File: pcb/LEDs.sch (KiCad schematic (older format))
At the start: 15 parts

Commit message: almost finished with pcb design
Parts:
- removed MATRIX? (x2): LED_8X8, symbol LED_8X8
- removed U? (x3): ULN2804A, symbol ULN2804A
- added MATRIX2, MATRIX3, MATRIX4: LED_8X8, symbol LED_8X8
- added RR17, RR18, RR19, RR20, RR21, RR22, RR23, RR24: 15, symbol R
- added U2: ULN2804A, symbol ULN2804A
- RR10, RR11, RR12, RR13, RR14, RR15, RR16, RR9: renamed from R?; value 82 -> 15
- gave numbers to parts that had none: 2
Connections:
- net labels added: C0, C1, C10, C11, C12, C13, C14, C2, C3, C4, C5, C6, C7, C8, C9, R0, R1, R2, R3, R4, R5, R6, R7
- wire segments 37 -> 118
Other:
- moved on the sheet: RR10, RR11, RR12, RR13, RR14, RR15, RR16, RR9, U1

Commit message: working on power circuitry
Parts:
- removed MATRIX1, MATRIX2, MATRIX3, MATRIX4: LED_8X8, symbol LED_8X8
- added MATRIX1: LED_16X16, symbol LED_16X16
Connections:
- wire segments 118 -> 86
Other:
- moved on the sheet: RR10, RR11, RR12, RR13, RR14, RR15, RR16, RR17, RR18, RR19, RR20, RR21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

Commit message: Work on single PCB version.
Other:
- moved on the sheet: U2
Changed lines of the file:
@@
-EESchema Schematic File Version 2  date Tue 12 Mar 2013 12:56:47 AM PDT
+EESchema Schematic File Version 2  date Tue 12 Mar 2013 12:36:21 PM PDT
 LIBS:power
 LIBS:device
@@
 LIBS:leaf
 LIBS:led_16x16
+LIBS:uA7800
 LIBS:panels_g4-cache
 EELAYER 25  0
@@
 Comment4 ""
 $EndDescr
+Wire Wire Line
+	3360 5480 3710 5480
+Wire Wire Line
+	7510 3185 7255 3185
+Wire Wire Line
+	7510 2985 7255 2985
+Wire Wire Line
+	7255 2785 7510 2785
+Wire Wire Line
+	7255 2585 7510 2585
+Wire Wire Line
+	7510 2685 7255 2685
+Wire Wire Line
+	7510 2885 7255 2885
+Wire Wire Line
+	7510 3085 7255 3085
+Wire Wire Line
+	7510 3285 7255 3285
+Wire Wire Line
+	7510 4085 7255 4085
+Wire Wire Line
+	7510 3885 7255 3885
+Wire Wire Line
+	7510 3685 7255 3685
+Wire Wire Line
+	7510 3485 7255 3485
+Wire Wire Line
+	7255 3385 7510 3385
+Wire Wire Line
+	7255 3585 7510 3585
+Wire Wire Line
+	7510 3785 7255 3785
+Wire Wire Line
+	7510 3985 7255 3985
+Wire Wire Line
+	3255 3385 3695 3385
+Wire Wire Line
+	5415 6150 5415 5980
+Wire Wire Line
+	5415 5980 5310 5980
+Wire Wire Line
+	4195 2685 4755 2685
+Wire Wire Line
+	4195 2785 4755 2785
+Wire Wire Line
+	4195 2985 4755 2985
+Wire Wire Line
+	4195 3085 4755 3085
+Wire Wire Line
+	4755 3185 4195 3185
+Wire Wire Line
+	4195 3285 4755 3285
+Wire Wire Line
+	4195 2885 4755 2885
+Wire Wire Line
+	4195 2585 4755 2585
+Wire Wire Line
+	3270 2585 3695 2585
+Wire Wire Line
+	3270 2685 3695 2685
+Wire Wire Line
+	3270 2785 3695 2785
+Wire Wire Line
+	3270 3085 3695 3085
+Wire Wire Line
+	3270 2985 3695 2985
+Wire Wire Line
+	3270 2885 3695 2885
+Wire Wire Line
+	3270 3185 3695 3185
+Wire Wire Line
+	3270 3285 3695 3285
+Wire Wire Line
+	3360 5880 3710 5880
+Wire Wire Line
+	3360 5780 3710 5780
+Wire Wire Line
+	3710 5580 3360 5580
+Wire Wire Line
+	3360 5680 3710 5680
+Wire Wire Line
+	3710 5380 3360 5380
+Wire Wire Line
+	3710 5280 3360 5280
+Wire Wire Line
+	3710 5180 3360 5180
+Wire Wire Line
+	5565 5880 5310 5880
+Wire Wire Line
+	5565 5680 5310 5680
+Wire Wire Line
+	5565 5480 5310 5480
+Wire Wire Line
+	5565 5280 5310 5280
+Wire Wire Line
+	5310 5180 5565 5180
+Wire Wire Line
+	5310 5380 5565 5380
+Wire Wire Line
+	5565 5580 5310 5580
+Wire Wire Line
+	5565 5780 5310 5780
+Wire Wire Line
+	4510 6580 4510 6730
+Wire Wire Line
+	7415 6525 7415 6675
+Wire Wire Line
+	8470 5725 8215 5725
+Wire Wire Line
+	8470 5525 8215 5525
+Wire Wire Line
+	8215 5325 8470 5325
+Wire Wire Line
+	8215 5125 8470 5125
+Wire Wire Line
+	8470 5225 8215 5225
+Wire Wire Line
+	8470 5425 8215 5425
+Wire Wire Line
+	8470 5625 8215 5625
+Wire Wire Line
+	8470 5825 8215 5825
+Wire Wire Line
+	6275 5125 6615 5125
+Wire Wire Line
+	6275 5225 6615 5225
+Wire Wire Line
+	6275 5325 6615 5325
+Wire Wire Line
+	6275 5625 6615 5625
+Wire Wire Line
+	6275 5525 6615 5525
+Wire Wire Line
+	6275 5425 6615 5425
+Wire Wire Line
+	6275 5725 6615 5725
+Wire Wire Line
+	6275 5825 6615 5825
+Wire Wire Line
+	8215 5925 8320 5925
+Wire Wire Line
+	8320 5925 8320 6095
+Wire Wire Line
+	3255 4085 3695 4085
+Wire Wire Line
+	3255 3985 3695 3985
+Wire Wire Line
+	3255 3685 3695 3685
+Wire Wire Line
+	3255 3785 3695 3785
+Wire Wire Line
+	3255 3885 3695 3885
+Wire Wire Line
+	3255 3585 3695 3585
+Wire Wire Line
+	3255 3485 3695 3485
+Wire Wire Line
+	4195 3385 4755 3385
+Wire Wire Line
+	4195 3685 4755 3685
+Wire Wire Line
+	4195 4085 4755 4085
+Wire Wire Line
+	4755 3985 4195 3985
+Wire Wire Line
+	4195 3885 4755 3885
+Wire Wire Line
+	4195 3785 4755 3785
+Wire Wire Line
+	4195 3585 4755 3585
+Wire Wire Line
+	4195 3485 4755 3485
+Text GLabel 3360 5280 0    60   Input ~ 0
+C6
 $Comp
 L LED_16X16 MATRIX1
@@
 	1    0    0    -1
 $EndComp
-Wire Wire Line
-	7510 3185 7255 3185
-Wire Wire Line
-	7510 2985 7255 2985
-Wire Wire Line
-	7255 2785 7510 2785
-Wire Wire Line
-	7255 2585 7510 2585
-Wire Wire Line
-	7510 2685 7255 2685
-Wire Wire Line
-	7510 2885 7255 2885
-Wire Wire Line
-	7510 3085 7255 3085
-Wire Wire Line
-	7510 3285 7255 3285
 Text Label 7510 2685 2    60   ~ 0
 C14
@@
 Text Label 7510 3285 2    60   ~ 0
 C8
-Wire Wire Line
-	7510 4085 7255 4085
-Wire Wire Line
-	7510 3885 7255 3885
-Wire Wire Line
-	7510 3685 7255 3685
-Wire Wire Line
-	7510 3485 7255 3485
-Wire Wire Line
-	7255 3385 7510 3385
-Wire Wire Line
-	7255 3585 7510 3585
-Wire Wire Line
-	7510 3785 7255 3785
-Wire Wire Line
-	7510 3985 7255 3985
 Text Label 7510 4085 2    60   ~ 0
 C0
@@
 Text Label 7510 3485 2    60   ~ 0
 C6
-Wire Wire Line
-	3255 3385 3695 3385
-Wire Wire Line
-	5415 6150 5415 5980
-Wire Wire Line
-	5415 5980 5310 5980
-Wire Wire Line
-	4195 2685 4755 2685
-Wire Wire Line
-	4195 2785 4755 2785
-Wire Wire Line
-	4195 2985 4755 2985
-Wire Wire Line
-	4195 3085 4755 3085
-Wire Wire Line
-	4755 3185 4195 3185
-Wire Wire Line
-	4195 3285 4755 3285
-Wire Wire Line
-	4195 2885 4755 2885
-Wire Wire Line
-	4195 2585 4755 2585
-Wire Wire Line
-	3270 2585 3695 2585
-Wire Wire Line
-	3270 2685 3695 2685
-Wire Wire Line
-	3270 2785 3695 2785
-Wire Wire Line
-	3270 3085 3695 3085
-Wire Wire Line
-	3270 2985 3695 2985
-Wire Wire Line
-	3270 2885 3695 2885
-Wire Wire Line
-	3270 3185 3695 3185
-Wire Wire Line
-	3270 3285 3695 3285
-Wire Wire Line
-	3490 5880 3710 5880
-Wire Wire Line
-	3490 5780 3710 5780
-Wire Wire Line
-	3490 5480 3710 5480
-Wire Wire Line
-	3490 5580 3710 5580
-Wire Wire Line
-	3490 5680 3710 5680
-Wire Wire Line
-	3490 5380 3710 5380
-Wire Wire Line
-	3490 5280 3710 5280
-Wire Wire Line
-	3490 5180 3710 5180
-Wire Wire Line
-	5565 5880 5310 5880
-Wire Wire Line
-	5565 5680 5310 5680
-Wire Wire Line
-	5565 5480 5310 5480
-Wire Wire Line
-	5565 5280 5310 5280
-Wire Wire Line
-	5310 5180 5565 5180
-Wire Wire Line
-	5310 5380 5565 5380
-Wire Wire Line
-	5565 5580 5310 5580
-Wire Wire Line
-	5565 5780 5310 5780
-Wire Wire Line
-	4510 6580 4510 6730
-Wire Wire Line
-	7295 6525 7295 6675
-Wire Wire Line
-	8350 5725 8095 5725
-Wire Wire Line
-	8350 5525 8095 5525
-Wire Wire Line
-	8095 5325 8350 5325
-Wire Wire Line
-	8095 5125 8350 5125
-Wire Wire Line
-	8350 5225 8095 5225
-Wire Wire Line
-	8350 5425 8095 5425
-Wire Wire Line
-	8350 5625 8095 5625
-Wire Wire Line
-	8350 5825 8095 5825
-Wire Wire Line
-	6275 5125 6495 5125
-Wire Wire Line
-	6275 5225 6495 5225
-Wire Wire Line
-	6275 5325 6495 5325
-Wire Wire Line
-	6275 5625 6495 5625
-Wire Wire Line
-	6275 5525 6495 5525
-Wire Wire Line
-	6275 5425 6495 5425
-Wire Wire Line
-	6275 5725 6495 5725
-Wire Wire Line
-	6275 5825 6495 5825
-Wire Wire Line
-	8095 5925 8200 5925
-Wire Wire Line
-	8200 5925 8200 6095
-Wire Wire Line
-	3255 4085 3695 4085
-Wire Wire Line
-	3255 3985 3695 3985
-Wire Wire Line
-	3255 3685 3695 3685
-Wire Wire Line
-	3255 3785 3695 3785
-Wire Wire Line
-	3255 3885 3695 3885
-Wire Wire Line
-	3255 3585 3695 3585
-Wire Wire Line
-	3255 3485 3695 3485
-Wire Wire Line
-	4195 3385 4755 3385
-Wire Wire Line
-	4195 3685 4755 3685
-Wire Wire Line
-	4195 4085 4755 4085
-Wire Wire Line
-	4755 3985 4195 3985
-Wire Wire Line
-	4195 3885 4755 3885
-Wire Wire Line
-	4195 3785 4755 3785
-Wire Wire Line
-	4195 3585 4755 3585
-Wire Wire Line
-	4195 3485 4755 3485
 $Comp
 L R RR17
@@
 L ULN2804A U2
 U 1 1 5110001A
-P 7295 5475
-F 0 "U2" H 7295 5975 60  0000 C CNN
-F 1 "ULN2804A" H 7295 6125 60  0000 C CNN
-	1    7295 5475
+P 7415 5475
+F 0 "U2" H 7415 5975 60  0000 C CNN
+F 1 "ULN2804A" H 7415 6125 60  0000 C CNN
+	1    7415 5475
 	1    0    0    -1
 $EndComp
@@
 L VCC #PWR014
 U 1 1 51100019
-P 8200 6095
-F 0 "#PWR014" H 8200 6195 30  0001 C CNN
-F 1 "VCC" H 8200 6195 30  0000 C CNN
-	1    8200 6095
+P 8320 6095
+F 0 "#PWR014" H 8320 6195 30  0001 C CNN
+F 1 "VCC" H 8320 6195 30  0000 C CNN
+	1    8320 6095
 	-1   0    0    1
 $EndComp
@@
 Text GLabel 6275 5125 0    60   Input ~ 0
 C15
-Text Label 8350 5225 2    60   ~ 0
+Text Label 8470 5225 2    60   ~ 0
 C14
-Text Label 8350 5125 2    60   ~ 0
+Text Label 8470 5125 2    60   ~ 0
 C15
-Text Label 8350 5325 2    60   ~ 0
+Text Label 8470 5325 2    60   ~ 0
 C13
-Text Label 8350 5425 2    60   ~ 0
+Text Label 8470 5425 2    60   ~ 0
 C12
-Text Label 8350 5525 2    60   ~ 0
+Text Label 8470 5525 2    60   ~ 0
 C11
-Text Label 8350 5625 2    60   ~ 0
+Text Label 8470 5625 2    60   ~ 0
 C10
-Text Label 8350 5725 2    60   ~ 0
+Text Label 8470 5725 2    60   ~ 0
 C9
-Text Label 8350 5825 2    60   ~ 0
+Text Label 8470 5825 2    60   ~ 0
 C8
 $Comp
 L GND #PWR015
 U 1 1 51100018
-P 7295 6675
-F 0 "#PWR015" H 7295 6675 30  0001 C CNN
-F 1 "GND" H 7295 6605 30  0001 C CNN
-	1    7295 6675
+P 7415 6675
+F 0 "#PWR015" H 7415 6675 30  0001 C CNN
+F 1 "GND" H 7415 6605 30  0001 C CNN
+	1    7415 6675
 	1    0    0    -1
 $EndComp
@@
 Text Label 5565 5280 2    60   ~ 0
 C6
-Text GLabel 3490 5180 0    60   Input ~ 0
+Text GLabel 3360 5180 0    60   Input ~ 0
 C7
-Text GLabel 3490 5280 0    60   Input ~ 0
-C6
-Text GLabel 3490 5380 0    60   Input ~ 0
+Text GLabel 3360 5380 0    60   Input ~ 0
 C5
-Text GLabel 3490 5680 0    60   Input ~ 0
+Text GLabel 3360 5680 0    60   Input ~ 0
 C2
-Text GLabel 3490 5580 0    60   Input ~ 0
+Text GLabel 3360 5580 0    60   Input ~ 0
 C3
-Text GLabel 3490 5480 0    60   Input ~ 0
+Text GLabel 3360 5480 0    60   Input ~ 0
 C4
-Text GLabel 3490 5780 0    60   Input ~ 0
+Text GLabel 3360 5780 0    60   Input ~ 0
 C1
-Text GLabel 3490 5880 0    60   Input ~ 0
+Text GLabel 3360 5880 0    60   Input ~ 0
 C0
 Text GLabel 3270 3285 0    60   Input ~ 0

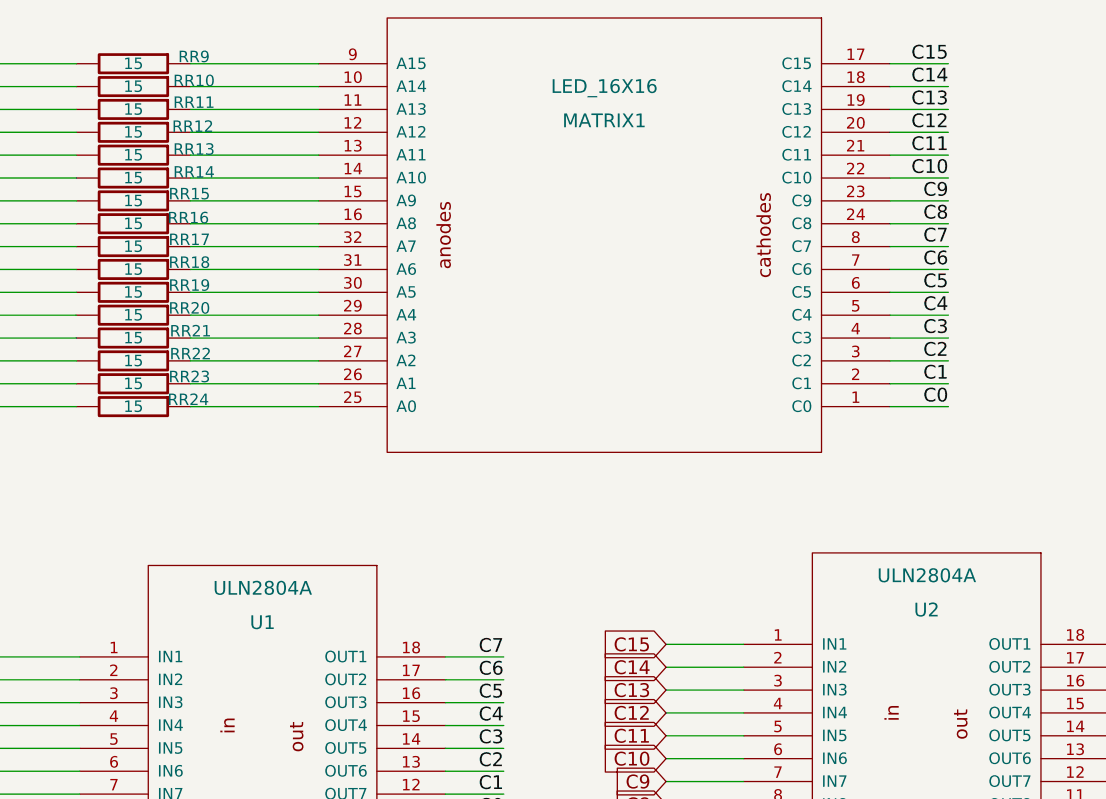
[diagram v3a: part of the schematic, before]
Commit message: Re-routing new, single-board PCB
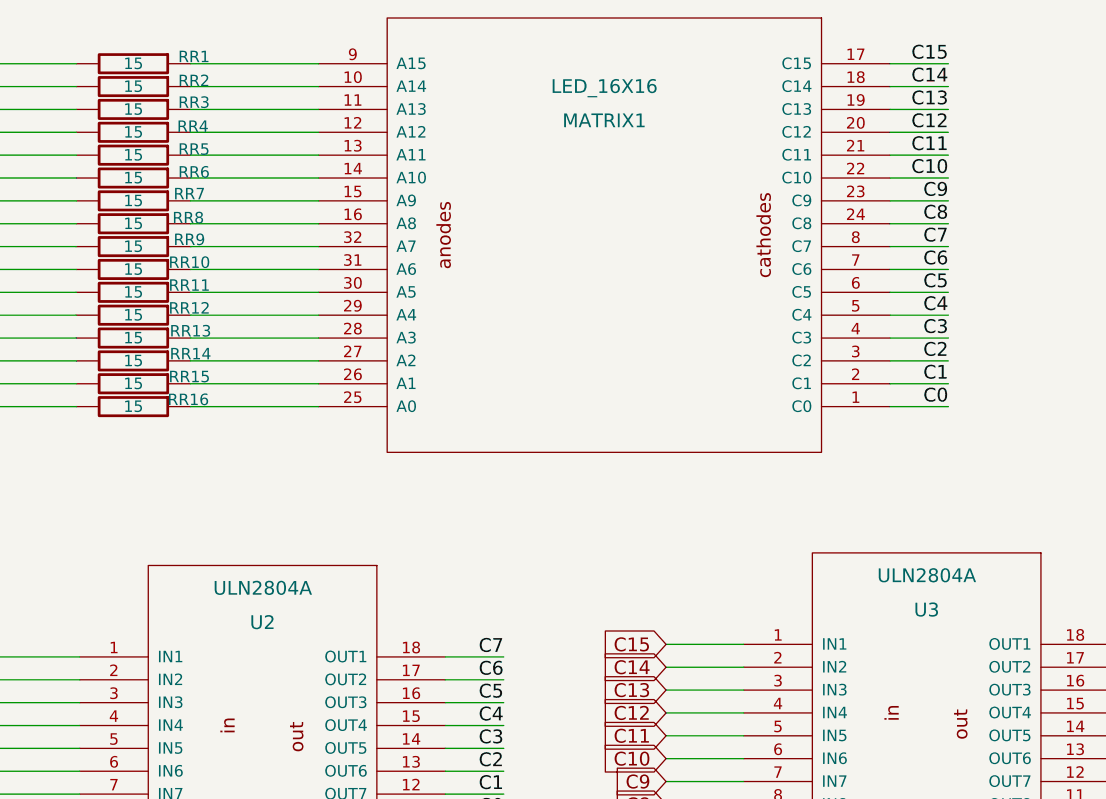
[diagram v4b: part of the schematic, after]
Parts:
- renumbered RR9 to RR1, RR18 to RR10, RR19 to RR11, RR20 to RR12, RR21 to RR13, RR22 to RR14, RR23 to RR15, RR24 to RR16, RR10 to RR2, RR11 to RR3, RR12 to RR4, RR13 to RR5, RR14 to RR6, RR15 to RR7, RR16 to RR8, RR17 to RR9, U1 to U2, U2 to U3
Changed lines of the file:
@@
-EESchema Schematic File Version 2  date Tue 12 Mar 2013 12:36:21 PM PDT
+EESchema Schematic File Version 2  date Wed 20 Mar 2013 06:41:12 PM PDT
 LIBS:power
 LIBS:device
@@
 Sheet 3 5
 Title ""
-Date "12 mar 2013"
+Date "21 mar 2013"
 Rev ""
 Comp ""
@@
 C6
 $Comp
-L R RR17
+L R RR9
 U 1 1 51100077
 P 3945 3385
-F 0 "RR17" V 3915 3630 50  0000 C CNN
+F 0 "RR9" V 3915 3630 50  0000 C CNN
 F 1 "15" V 3945 3385 50  0000 C CNN
 	1    3945 3385
@@
 $EndComp
 $Comp
-L R RR23
+L R RR15
 U 1 1 51100076
 P 3945 3985
-F 0 "RR23" V 3915 4230 50  0000 C CNN
+F 0 "RR15" V 3915 4230 50  0000 C CNN
 F 1 "15" V 3945 3985 50  0000 C CNN
 	1    3945 3985
@@
 $EndComp
 $Comp
-L R RR24
+L R RR16
 U 1 1 51100075
 P 3945 4085
-F 0 "RR24" V 3915 4325 50  0000 C CNN
+F 0 "RR16" V 3915 4325 50  0000 C CNN
 F 1 "15" V 3945 4085 50  0000 C CNN
 	1    3945 4085
@@
 $EndComp
 $Comp
-L R RR22
+L R RR14
 U 1 1 51100074
 P 3945 3885
-F 0 "RR22" V 3915 4135 50  0000 C CNN
+F 0 "RR14" V 3915 4135 50  0000 C CNN
 F 1 "15" V 3945 3885 50  0000 C CNN
 	1    3945 3885
@@
 $EndComp
 $Comp
-L R RR21
+L R RR13
 U 1 1 51100073
 P 3945 3785
-F 0 "RR21" V 3915 4035 50  0000 C CNN
+F 0 "RR13" V 3915 4035 50  0000 C CNN
 F 1 "15" V 3945 3785 50  0000 C CNN
 	1    3945 3785
@@
 $EndComp
 $Comp
-L R RR19
+L R RR11
 U 1 1 51100072
 P 3945 3585
-F 0 "RR19" V 3915 3830 50  0000 C CNN
+F 0 "RR11" V 3915 3830 50  0000 C CNN
 F 1 "15" V 3945 3585 50  0000 C CNN
 	1    3945 3585
@@
 $EndComp
 $Comp
-L R RR20
+L R RR12
 U 1 1 51100071
 P 3945 3685
-F 0 "RR20" V 3915 3930 50  0000 C CNN
+F 0 "RR12" V 3915 3930 50  0000 C CNN
 F 1 "15" V 3945 3685 50  0000 C CNN
 	1    3945 3685
@@
 $EndComp
 $Comp
-L R RR18
+L R RR10
 U 1 1 51100070
 P 3945 3485
-F 0 "RR18" V 3915 3730 50  0000 C CNN
+F 0 "RR10" V 3915 3730 50  0000 C CNN
 F 1 "15" V 3945 3485 50  0000 C CNN
 	1    3945 3485
@@
 R0
 $Comp
-L ULN2804A U2
+L ULN2804A U3
 U 1 1 5110001A
 P 7415 5475
-F 0 "U2" H 7415 5975 60  0000 C CNN
+F 0 "U3" H 7415 5975 60  0000 C CNN
 F 1 "ULN2804A" H 7415 6125 60  0000 C CNN
 	1    7415 5475
@@
 $EndComp
 $Comp
-L VCC #PWR014
+L VCC #PWR015
 U 1 1 51100019
 P 8320 6095
-F 0 "#PWR014" H 8320 6195 30  0001 C CNN
+F 0 "#PWR015" H 8320 6195 30  0001 C CNN
 F 1 "VCC" H 8320 6195 30  0000 C CNN
 	1    8320 6095
@@
 C8
 $Comp
-L GND #PWR015
+L GND #PWR016
 U 1 1 51100018
 P 7415 6675
-F 0 "#PWR015" H 7415 6675 30  0001 C CNN
+F 0 "#PWR016" H 7415 6675 30  0001 C CNN
 F 1 "GND" H 7415 6605 30  0001 C CNN
 	1    7415 6675
@@
 $EndComp
 $Comp
-L GND #PWR016
+L GND #PWR017
 U 1 1 51099CA6
 P 4510 6730
-F 0 "#PWR016" H 4510 6730 30  0001 C CNN
+F 0 "#PWR017" H 4510 6730 30  0001 C CNN
 F 1 "GND" H 4510 6660 30  0001 C CNN
 	1    4510 6730
@@
 R15
 $Comp
-L VCC #PWR017
+L VCC #PWR018
 U 1 1 51099CA5
 P 5415 6150
-F 0 "#PWR017" H 5415 6250 30  0001 C CNN
+F 0 "#PWR018" H 5415 6250 30  0001 C CNN
 F 1 "VCC" H 5415 6250 30  0000 C CNN
 	1    5415 6150
@@
 $EndComp
 $Comp
-L ULN2804A U1
+L ULN2804A U2
 U 1 1 51099CA4
 P 4510 5530
-F 0 "U1" H 4510 6030 60  0000 C CNN
+F 0 "U2" H 4510 6030 60  0000 C CNN
 F 1 "ULN2804A" H 4510 6180 60  0000 C CNN
 	1    4510 5530
@@
 $EndComp
 $Comp
-L R RR10
+L R RR2
 U 1 1 51087F2A
 P 3945 2685
-F 0 "RR10" V 3920 2950 50  0000 C CNN
+F 0 "RR2" V 3920 2950 50  0000 C CNN
 F 1 "15" V 3945 2685 50  0000 C CNN
 	1    3945 2685
@@
 $EndComp
 $Comp
-L R RR12
+L R RR4
 U 1 1 51087F29
 P 3945 2885
-F 0 "RR12" V 3920 3145 50  0000 C CNN
+F 0 "RR4" V 3920 3145 50  0000 C CNN
 F 1 "15" V 3945 2885 50  0000 C CNN
 	1    3945 2885
@@
 $EndComp
 $Comp
-L R RR11
+L R RR3
 U 1 1 51087F28
 P 3945 2785
-F 0 "RR11" V 3915 3050 50  0000 C CNN
+F 0 "RR3" V 3915 3050 50  0000 C CNN
 F 1 "15" V 3945 2785 50  0000 C CNN
 	1    3945 2785
@@
 $EndComp
 $Comp
-L R RR13
+L R RR5
 U 1 1 51087F27
 P 3945 2985
-F 0 "RR13" V 3920 3250 50  0000 C CNN
+F 0 "RR5" V 3920 3250 50  0000 C CNN
 F 1 "15" V 3945 2985 50  0000 C CNN
 	1    3945 2985
@@
 $EndComp
 $Comp
-L R RR14
+L R RR6
 U 1 1 51087F26
 P 3945 3085
-F 0 "RR14" V 3920 3350 50  0000 C CNN
+F 0 "RR6" V 3920 3350 50  0000 C CNN
 F 1 "15" V 3945 3085 50  0000 C CNN
 	1    3945 3085
@@
 $EndComp
 $Comp
-L R RR16
+L R RR8
 U 1 1 51087F22
 P 3945 3285
-F 0 "RR16" V 3920 3525 50  0000 C CNN
+F 0 "RR8" V 3920 3525 50  0000 C CNN
 F 1 "15" V 3945 3285 50  0000 C CNN
 	1    3945 3285
@@
 $EndComp
 $Comp
-L R RR15
+L R RR7
 U 1 1 51087F21
 P 3945 3185
-F 0 "RR15" V 3915 3430 50  0000 C CNN
+F 0 "RR7" V 3915 3430 50  0000 C CNN
 F 1 "15" V 3945 3185 50  0000 C CNN
 	1    3945 3185
@@
 $EndComp
 $Comp
-L R RR9
+L R RR1
 U 1 1 51087F1F
 P 3945 2585
-F 0 "RR9" V 3915 2850 50  0000 C CNN
+F 0 "RR1" V 3915 2850 50  0000 C CNN
 F 1 "15" V 3945 2585 50  0000 C CNN
 	1    3945 2585
